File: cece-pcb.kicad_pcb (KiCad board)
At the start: 2 copper layers, 67.3 x 94.8 mm, 46 parts, among them J101 SERIAL, J103 Conn_01x03_Male, J201 VAC, J202 Conn_01x03_Female, K201 SANYOU_SRD_Form_C, Q201 Q_NPN, SW101 SW_Push, SW102 SW_Push, U101 TLV75533PDBV, U102 ESP-12F/ESP07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

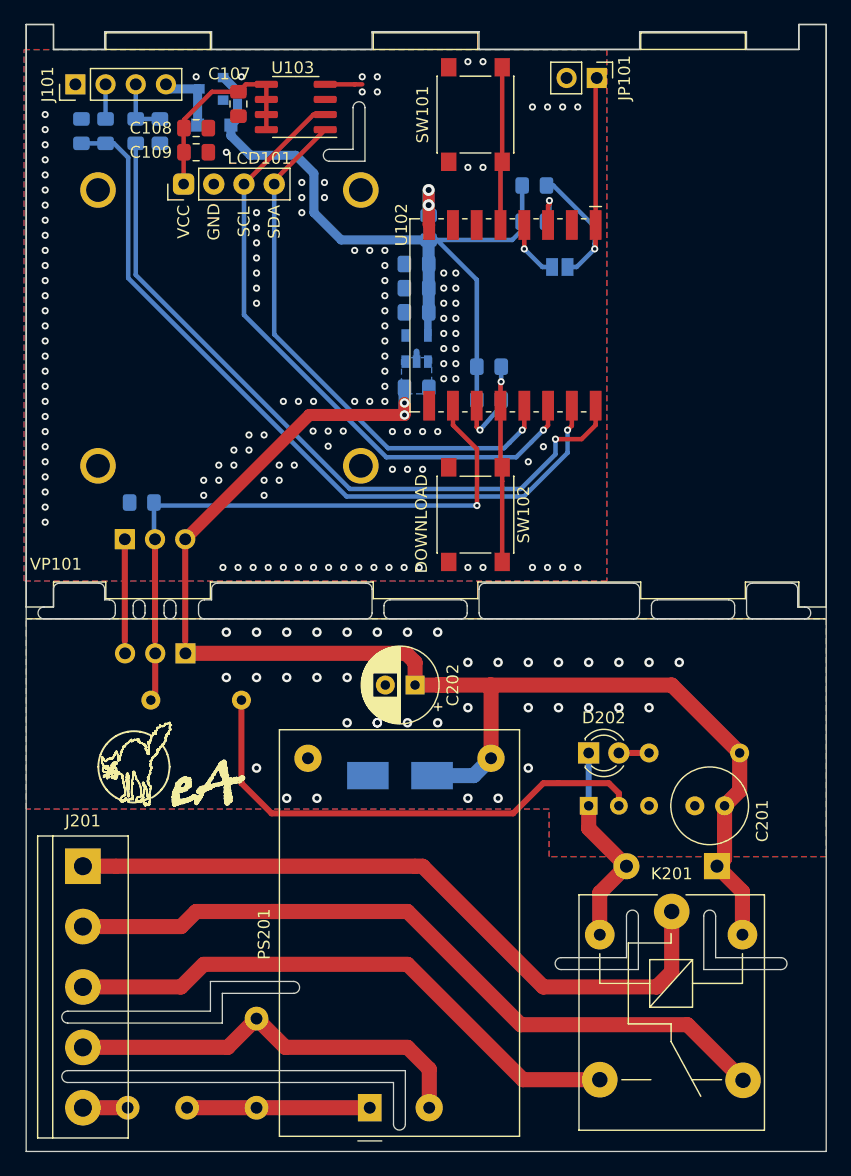
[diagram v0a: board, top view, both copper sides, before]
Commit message: Fix minor PCB mistakes and bump up the version to 1.01
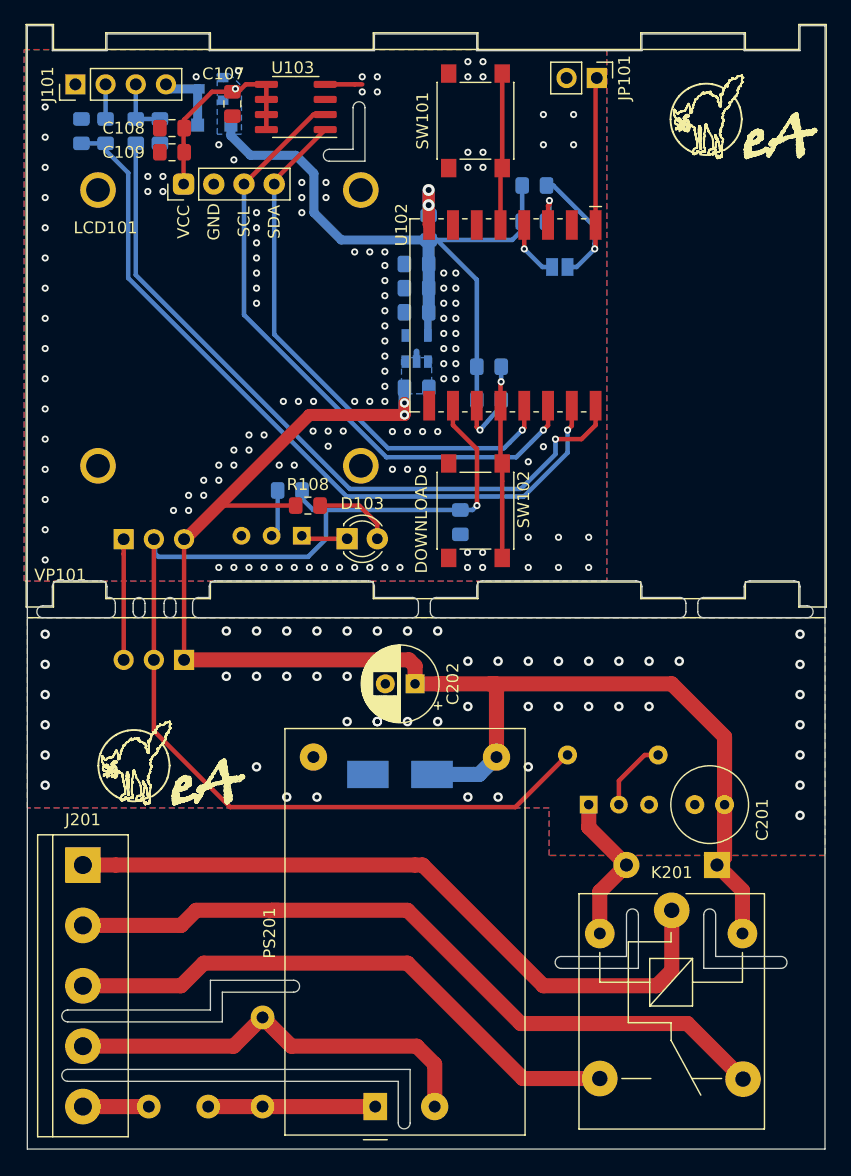
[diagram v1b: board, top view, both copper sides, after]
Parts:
- removed D202: LED, LED_THT:LED_D3.0mm
- removed R201: 220, Resistor_THT:R_Axial_DIN0207_L6.3mm_D2.5mm_P7.62mm_Horizontal
- added D103: LED, LED_THT:LED_D3.0mm, F.Cu at (127.0, 64.3)
- added Q101: Q_NPN, Package_TO_SOT_THT:TO-92L_Inline_Wide, B.Cu at (123.2, 64.0)
- added R108: 330, Resistor_SMD:R_0805_2012Metric_Pad1.15x1.40mm_HandSolder, F.Cu at (123.7, 61.5)
- added R109: 10k, Resistor_SMD:R_0805_2012Metric_Pad1.15x1.40mm_HandSolder, B.Cu at (122.2, 60.2)
- EA101: moved to F.Cu
- moved R202 35.4 mm to (153.2, 82.5)
- moved R106 26.8 mm to (136.5, 62.9), turned to 90 degrees
- moved EA101 6.43 mm to (154.2, 32.3)
- moved C108 2.03 mm to (112.3, 29.7), turned to 180 degrees
- moved C109 2.03 mm to (112.3, 31.8), turned to 180 degrees
- moved F201 1.78 mm to (115.3, 112.0)
- moved J202 0.56 mm to (113.3, 74.4)
- moved SW101 0.53 mm to (137.8, 29.1)
- moved RV201 0.52 mm to (119.9, 112.0)
- moved C107 0.51 mm to (117.3, 27.7)
- moved PS201 0.47 mm to (129.4, 112.0)
- moved SW102 0.33 mm to (137.8, 61.9)
- moved D201 0.10 mm to (158.1, 91.7)
- moved D203 0.10 mm to (131.4, 84.1)
- moved J201 0.10 mm to (104.8, 91.7)
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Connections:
- net /D8 renamed D8
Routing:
- net D8: track 52.3 -> 100.1 mm
- net Net-(Q201-Pad2): track 42.2 -> 6.21 mm
- net +5V: track 116.5 -> 127.8 mm
- net Net-(D103-Pad2): track 0.00 -> 6.72 mm
- net +3V3: track 80.8 -> 76.4 mm, vias 0 -> 1
- net Net-(D201-Pad2): track 17.5 -> 13.1 mm
- net Net-(Q101-Pad2): track 0.00 -> 4.03 mm
- net Net-(D103-Pad1): track 0.00 -> 3.81 mm
- net Net-(D202-Pad2): track 2.54 -> 0.00 mm
- net /Bottom Board/ACL: track 3.76 -> 5.54 mm
- net GND: track 13.9 -> 15.6 mm, vias 174 -> 187
- net Net-(F201-Pad1): track 15.5 -> 14.2 mm
- net /Bottom Board/ACN: track 35.1 -> 35.8 mm
- added copper zone on B.Cu, net +3V3
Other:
- board size 67.3 x 94.8 mm -> 67.1 x 94.5 mm
- board text added: "cece-1.01"

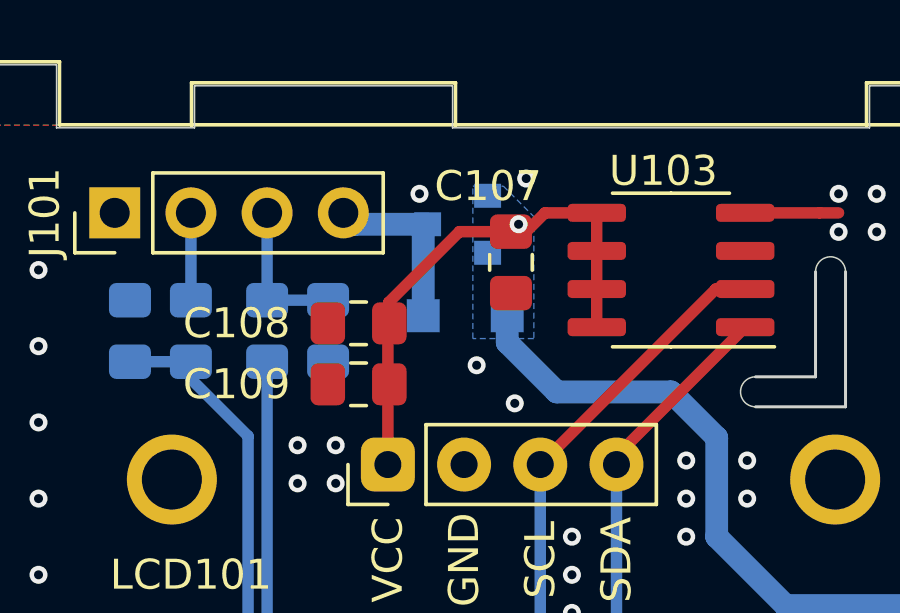
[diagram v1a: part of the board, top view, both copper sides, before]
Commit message: Fix diode in the wrong direction and increase PCB revision to 1.02
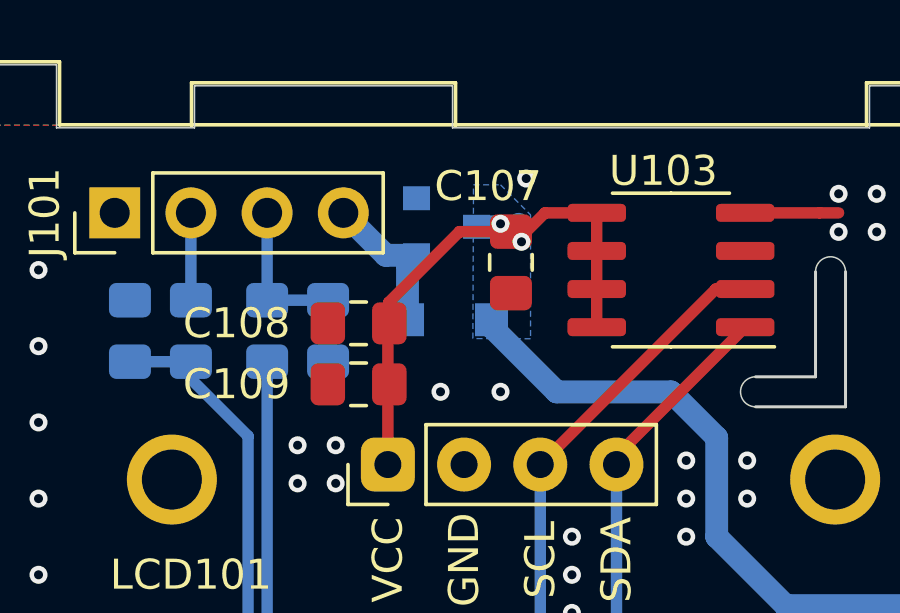
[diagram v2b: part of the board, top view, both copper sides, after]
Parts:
- moved D102 0.54 mm to (115.3, 29.6), turned to 180 degrees
- moved D101 0.38 mm to (115.2, 26.5), turned to 0 degrees
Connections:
- D101 pad 1: Net-(D101-Pad1) -> +3V3
- D101 pad 2: +3V3 -> Net-(D101-Pad2)
- D102 pad 1: Net-(D101-Pad1) -> +3V3
- D102 pad 2: +3V3 -> Net-(D101-Pad2)
- J101 pad 4: Net-(D101-Pad1) -> Net-(D101-Pad2)
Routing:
- net Net-(D101-Pad1): track 6.08 -> 0.00 mm
- net Net-(D101-Pad2): track 0.00 -> 5.30 mm
- net +3V3: track 76.4 -> 77.8 mm, vias 1 -> 2
- net GND: vias 187 -> 186
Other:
- board text added: "cece-1.02 BOTTOM"
- board text added: "cece-1.02 TOP"
- board text removed: "cece-1.01"

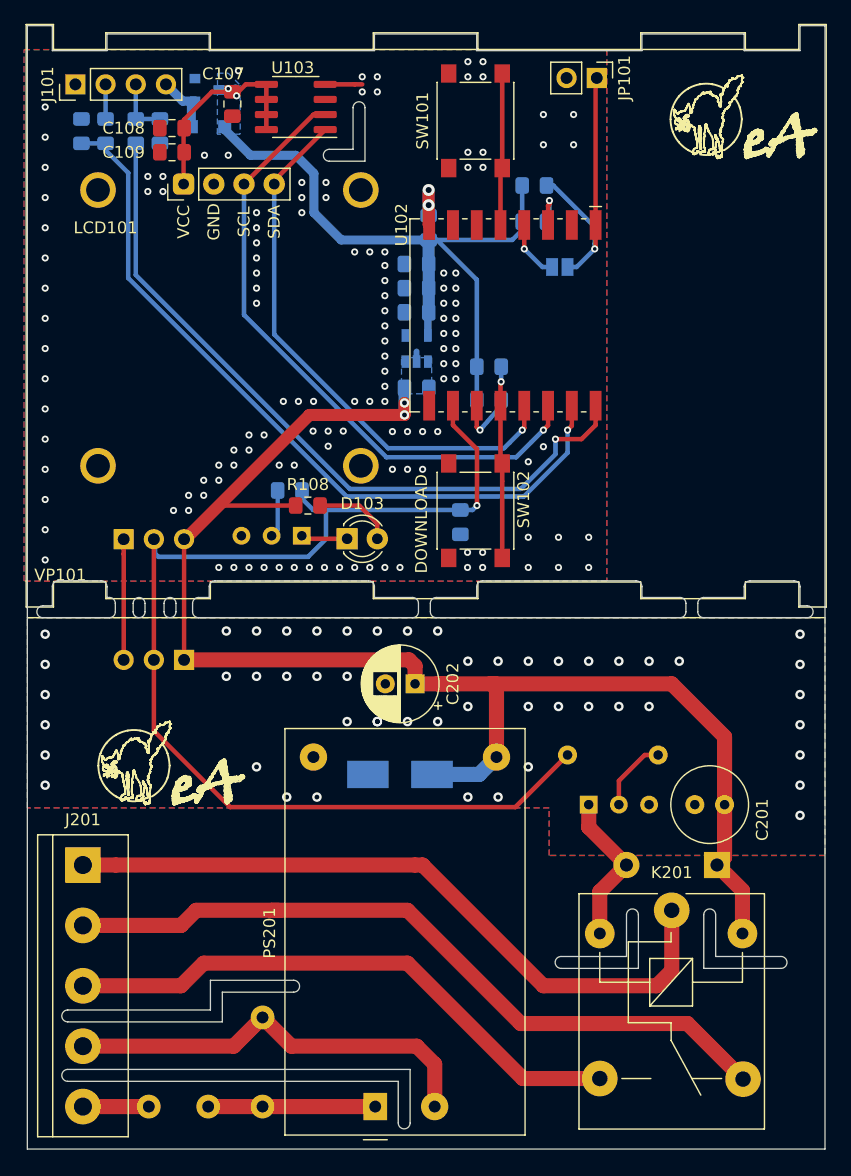
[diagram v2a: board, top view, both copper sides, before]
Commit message: Update project to kicad 6 and move some components around
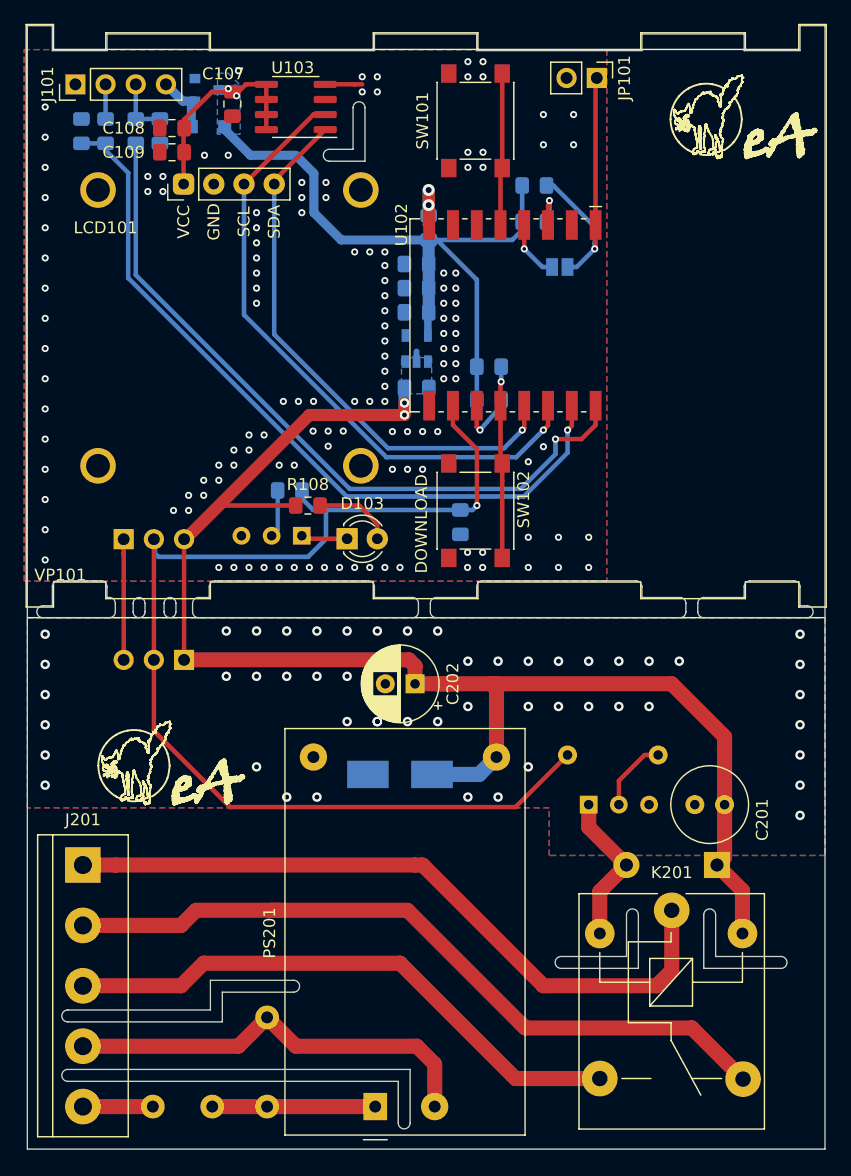
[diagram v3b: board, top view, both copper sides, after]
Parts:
- moved RV201 0.38 mm to (120.3, 112.0)
- moved F201 0.34 mm to (115.7, 112.0)
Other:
- net class Default removed
